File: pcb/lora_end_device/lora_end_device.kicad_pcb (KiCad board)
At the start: 2 copper layers, 61 x 41.5 mm, 31 parts, among them J1 USB_B_Micro, J2 UFL, J3 SMA, J4 UART, J5 Reset, J6 PRG, J7 Sensor, U2 MCP6021, U3 LD1117, U4 RFM95W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

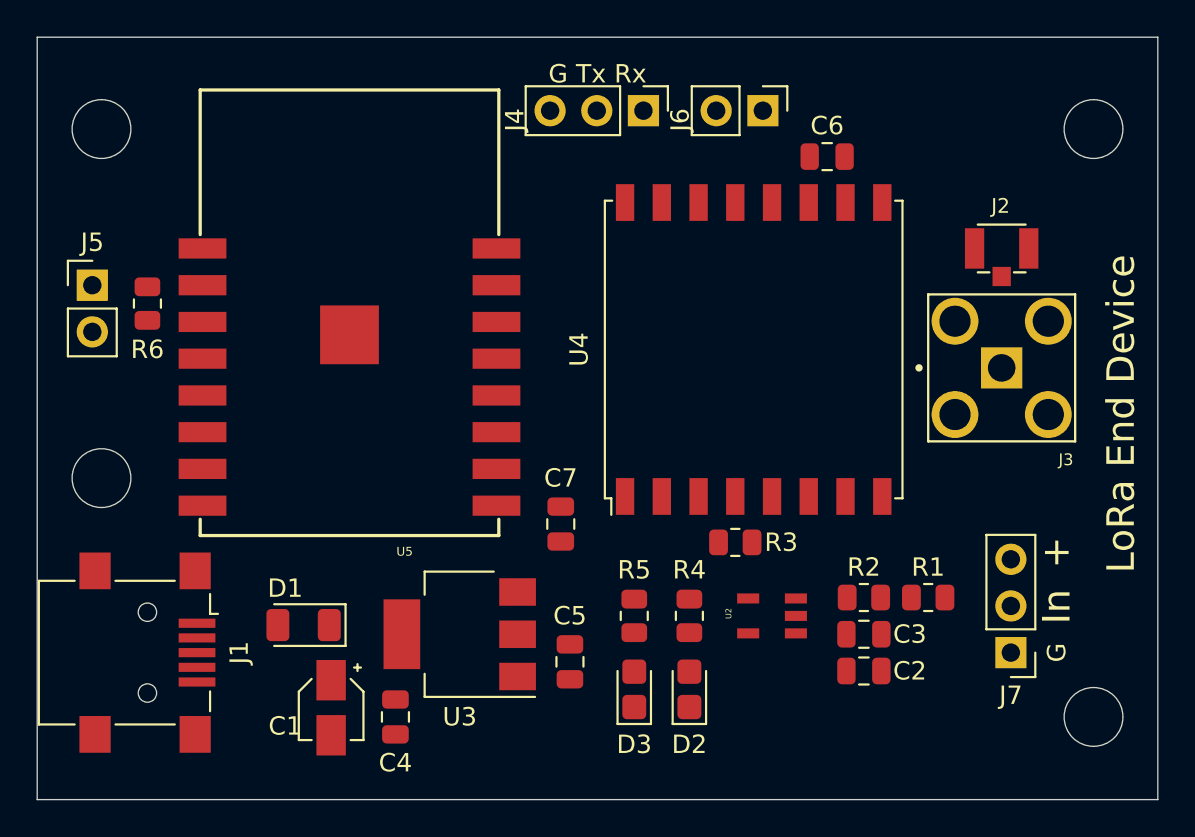
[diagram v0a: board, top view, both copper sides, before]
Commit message: reubicacion de U5 y U4
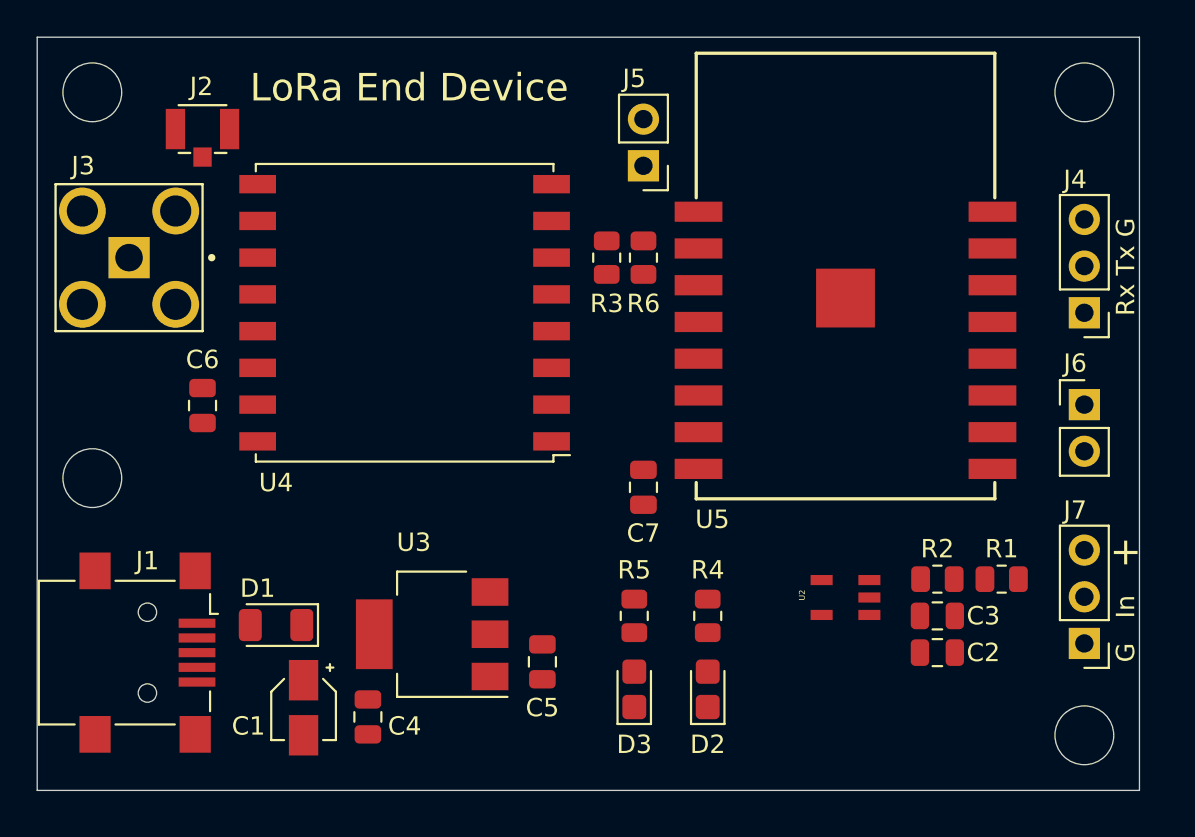
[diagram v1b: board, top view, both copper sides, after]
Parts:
- moved J3 47.9 mm to (63.0, 70.0), turned to 270 degrees
- moved J2 44.0 mm to (67.0, 63.0)
- moved C6 36.6 mm to (67.0, 78.0), turned to 270 degrees
- moved J5 30.7 mm to (91.0, 65.0), turned to 180 degrees
- moved R6 27.1 mm to (91.0, 70.0)
- moved U5 27.1 mm to (102.0, 71.0)
- moved J4 26.4 mm to (115.0, 73.0), turned to 180 degrees
- moved J6 23.7 mm to (115.0, 78.0), turned to 0 degrees
- moved U4 19.1 mm to (78.0, 73.0), turned to 180 degrees
- moved R3 17.0 mm to (89.0, 70.0), turned to 270 degrees
- moved C7 4.92 mm to (91.0, 82.5), turned to 270 degrees
- moved C2 4.12 mm to (107.0, 91.5)
- moved C3 4.12 mm to (107.0, 89.5)
- moved R1 4.12 mm to (110.5, 87.5)
- moved R2 4.12 mm to (107.0, 87.5)
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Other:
- board size 61 x 41.5 mm -> 60 x 41 mm
- board text added: "Rx Tx G"
- board text removed: "G Tx Rx"
